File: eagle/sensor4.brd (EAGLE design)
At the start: 46.5 x 44.4 mm, 15 parts, among them X1 1503_02, X2 io, X3 1503_02

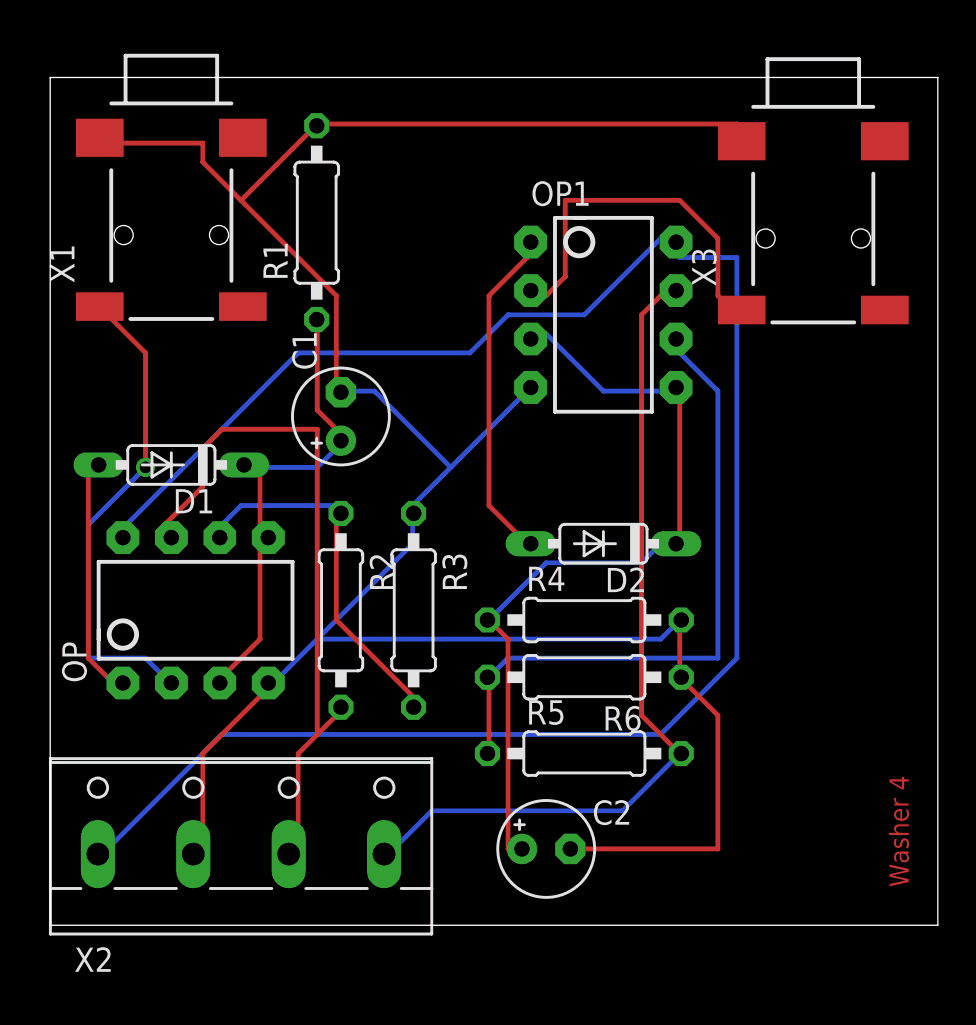
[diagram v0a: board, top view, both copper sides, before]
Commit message: Reshaped the board slightly more sensibly
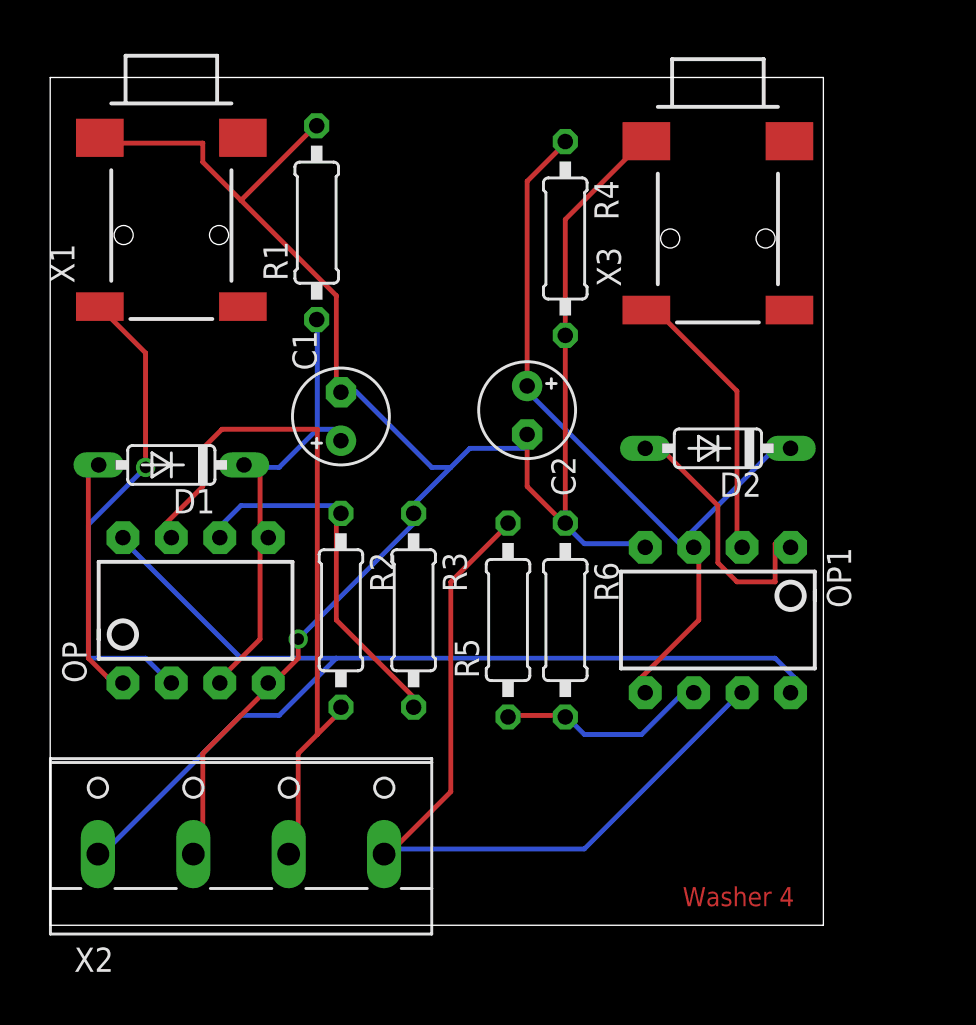
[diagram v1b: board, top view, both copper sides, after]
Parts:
- moved C2 23.0 mm to (25.0, 27.0), turned to 270 degrees
- moved R4 20.0 mm to (27.0, 36.0), turned to 270 degrees
- moved OP1 17.1 mm to (35.0, 16.0), turned to 180 degrees
- moved R5 8.06 mm to (24.0, 16.0), turned to 90 degrees
- moved D2 7.81 mm to (35.0, 25.0)
- moved X3 5.00 mm to (35.0, 43.0)
- moved R6 3.16 mm to (27.0, 16.0), turned to 270 degrees
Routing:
- net +3V3: track 98.3 -> 55.8 mm
- net GND: track 129.9 -> 98.2 mm, vias 0 -> 1
- net N$8: track 34.2 -> 11.2 mm
- net N$9: track 19.9 -> 14.8 mm
- net N$3: track 17.7 -> 14.3 mm
- net N$10: track 43.9 -> 42.3 mm
- net N$4: track 42.2 -> 42.8 mm
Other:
- board size 46.5 x 44.4 mm -> 40.5 x 44.4 mm

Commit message: Switch to separate header pin set for signal
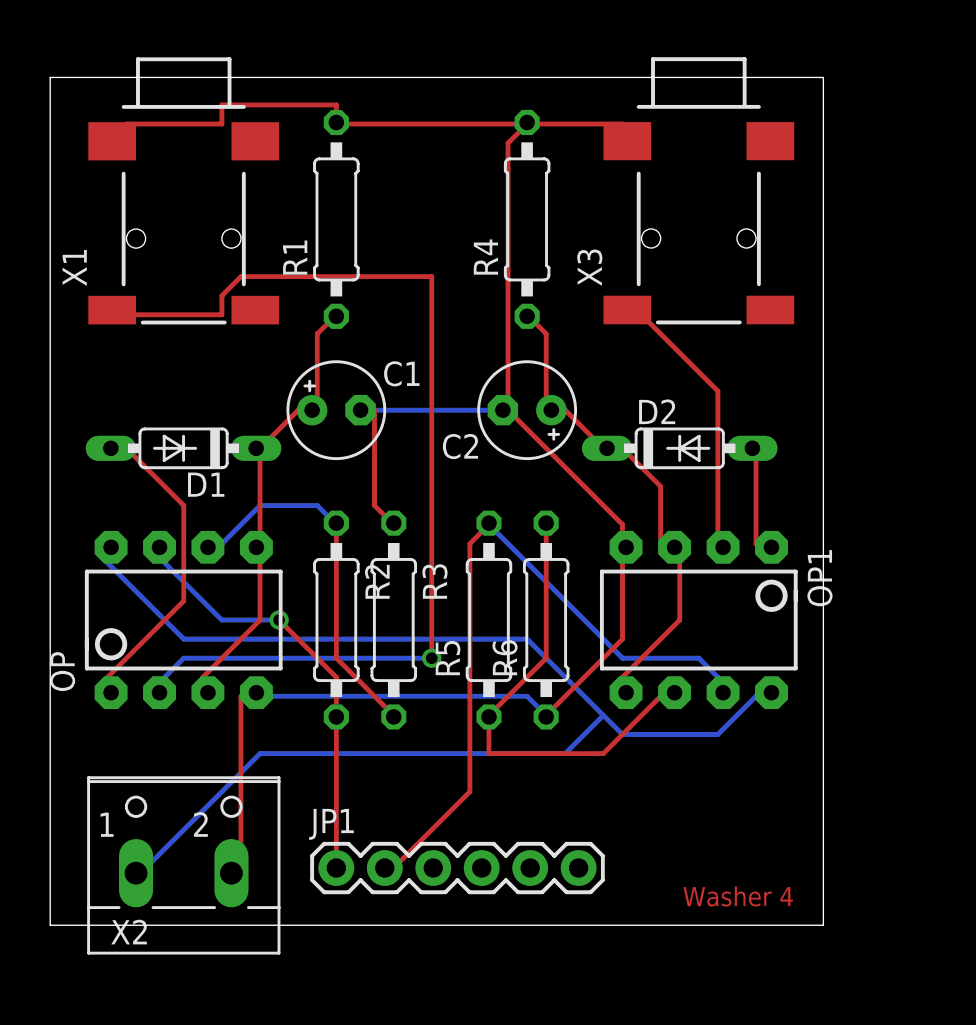
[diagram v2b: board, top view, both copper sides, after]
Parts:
- added JP1: (no value), SparkFun-Connectors:1X06
- X2: value io -> (none); device con-wago-500:W237-4 -> con-wago-500:W237-102
- moved X2 3.16 mm to (7.00, 4.00)
- moved R4 2.24 mm to (25.0, 37.0), turned to 90 degrees
- moved D2 2.00 mm to (33.0, 25.0), turned to 0 degrees
- moved R3 1.16 mm to (18.0, 16.0)
- moved D1 1.08 mm to (6.99, 25.0)
- moved R1 1.04 mm to (15.0, 37.0)
- moved OP1 1.00 mm to (34.0, 16.0)
- moved R5 1.00 mm to (23.0, 16.0)
- moved R6 1.00 mm to (26.0, 16.0), turned to 90 degrees
- moved X3 1.00 mm to (34.0, 43.0)
- moved OP 0.80 mm to (7.00, 16.0)
- moved X1 0.68 mm to (7.00, 43.0)
- moved R2 0.56 mm to (15.0, 16.0)
- moved C1 0.41 mm to (15.0, 27.0), turned to 0 degrees
- turned C2 to 180 degrees
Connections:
- net N$10: now also JP1.2; no longer X2.4
- net N$7: now also JP1.1; no longer X2.3
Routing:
- net N$6: track 25.5 -> 53.5 mm
- net N$4: track 42.8 -> 25.8 mm
- net N$7: track 36.9 -> 22.3 mm, vias 0 -> 1
- net N$8: track 11.2 -> 24.3 mm
- net +3V3: track 55.8 -> 68.1 mm
- net GND: track 98.2 -> 107.0 mm, vias 1 -> 0
- net N$3: track 14.3 -> 6.02 mm
- net N$10: track 42.3 -> 36.9 mm
- net N$1: track 12.8 -> 16.6 mm
- net N$2: track 25.9 -> 23.7 mm

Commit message: Replace two LM358s with one LMV324
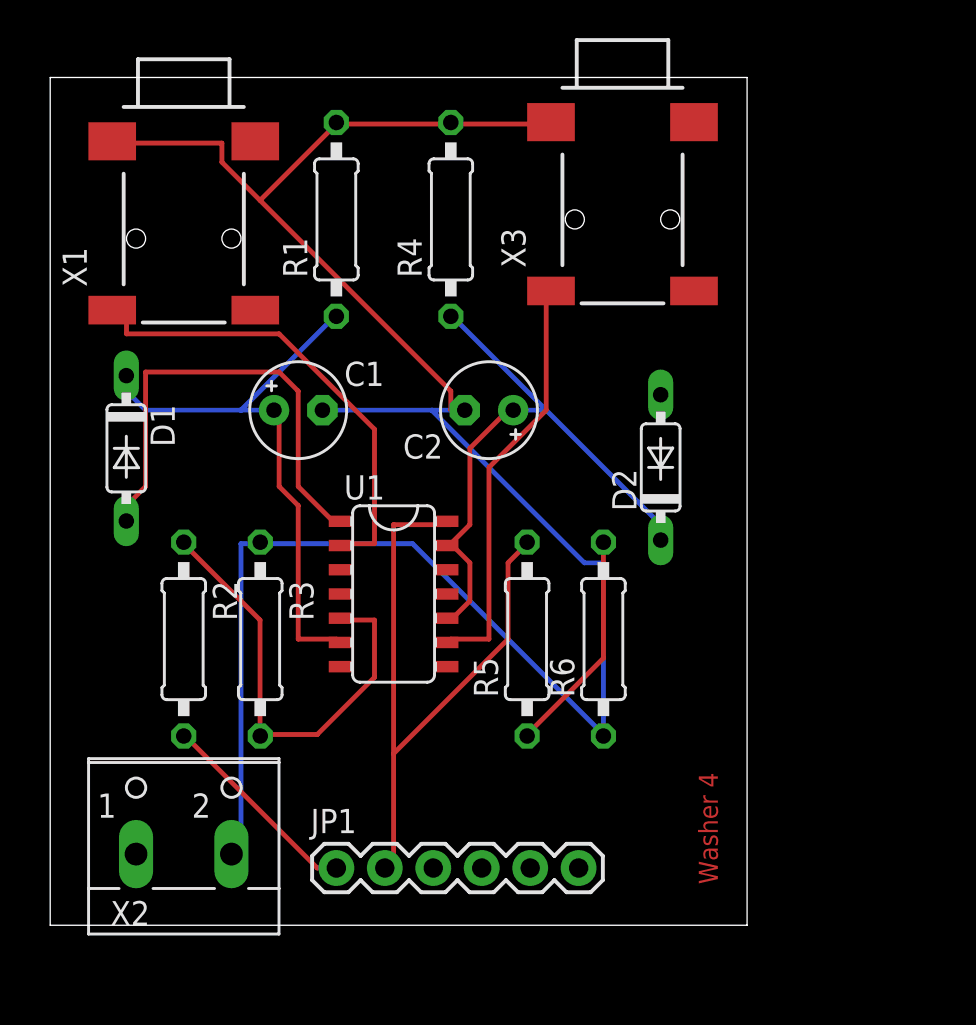
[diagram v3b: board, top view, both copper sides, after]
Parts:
- removed OP, OP1: LM358, SparkFun-AnalogIC:DIP08
- added U1: LMV324, SparkFun-AnalogIC:SO014
- moved R2 8.06 mm to (7.00, 15.0)
- moved R3 7.07 mm to (11.0, 15.0)
- moved X3 4.12 mm to (30.0, 44.0)
- moved R4 4.00 mm to (21.0, 37.0)
- moved R6 3.16 mm to (29.0, 15.0)
- moved D1 3.00 mm to (3.99, 25.0), turned to 270 degrees
- moved R5 2.24 mm to (25.0, 15.0)
- moved C1 2.00 mm to (13.0, 27.0)
- moved C2 2.00 mm to (23.0, 27.0)
- moved D2 1.41 mm to (32.0, 24.0), turned to 90 degrees
- moved X2 1.00 mm to (7.00, 5.00)
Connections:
- net +3V3: now also U1.4; no longer OP.8, OP1.8
- net GND: now also U1.11; no longer OP.4, OP1.4
- net N$1: now also U1.1; no longer OP.1
- net N$10: now also U1.14; no longer OP1.7
- net N$2: now also U1.3, U1.6; no longer OP.3, OP.5
- net N$3: now also U1.8; no longer OP1.1
- net N$4: now also U1.10, U1.13; no longer OP1.3, OP1.5
- net N$5: now also U1.5; no longer OP.6
- net N$6: now also U1.2; no longer OP.2
- net N$7: now also U1.7; no longer OP.7
- net N$8: now also U1.12; no longer OP1.6
- net N$9: now also U1.9; no longer OP1.2
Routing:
- net +3V3: track 68.1 -> 0.00 mm
- net N$6: track 53.5 -> 25.1 mm, vias 1 -> 0
- net N$8: track 24.3 -> 11.8 mm
- net N$7: track 22.3 -> 11.0 mm, vias 1 -> 0
- net N$1: track 16.6 -> 24.7 mm
- net N$2: track 23.7 -> 31.1 mm
- net N$9: track 14.8 -> 21.9 mm
- net N$4: track 25.8 -> 32.0 mm
- net N$3: track 6.02 -> 0.00 mm
- net N$5: track 19.5 -> 24.3 mm
- net GND: track 107.0 -> 111.2 mm
- net N$10: track 36.9 -> 35.7 mm
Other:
- board size 40.5 x 44.4 mm -> 36.5 x 44.4 mm
